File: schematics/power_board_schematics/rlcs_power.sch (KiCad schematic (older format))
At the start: 40 parts, among them J1 SD_Card, J2 Battery Conn, J3 CONN_01X02, J4 CONN_01X02, J5 CONN_01X02, J6 CONN_01X02, Q4 Q_NPN_BEC, Q5 Q_NPN_BEC, T1 12 to 3v3, T2 12 to 5

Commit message: Added more connections
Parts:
- renumbered Header to Header1
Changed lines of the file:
@@
 $EndComp
-$Comp
-L Device:R_Small R2
-U 1 1 59C44DB4
-P 3450 4900
-F 0 "R2" V 3450 4850 50  0000 L CNN
-F 1 "150" V 3500 4850 50  0001 L CNN
-F 2 "Resistors_SMD:R_0805_HandSoldering" H 3450 4900 50  0001 C CNN
-F 3 "" H 3450 4900 50  0001 C CNN
-	1    3450 4900
-	0    -1   -1   0
-$EndComp
-Text Notes 3200 4800 0    60   ~ 0
-100ohm\nresistors\n
 $Comp
 L Device:Jumper_NC_Dual JP1
@@
 	1    4750 1350
 	1    0    0    -1
-$EndComp
-$Comp
-L Device:R_Small R3
-U 1 1 59C5B971
-P 3450 5000
-F 0 "R3" V 3450 4950 50  0000 L CNN
-F 1 "150" V 3500 4950 50  0001 L CNN
-F 2 "Resistors_SMD:R_0805_HandSoldering" H 3450 5000 50  0001 C CNN
-F 3 "" H 3450 5000 50  0001 C CNN
-	1    3450 5000
-	0    -1   -1   0
-$EndComp
-$Comp
-L custom:LTD-4608JR AFF1
-U 1 1 59C5BADA
-P 4300 5300
-F 0 "AFF1" H 3950 4800 50  0000 C CNN
-F 1 "LTD-4608JR" H 4600 4800 50  0000 C CNN
-F 2 "rlcs_power:LTD-4608JR" H 4300 5300 50  0001 C CNN
-F 3 "" H 4300 5300 50  0001 C CNN
-	1    4300 5300
-	0    -1   -1   0
-$EndComp
-$Comp
-L Device:R_Small R4
-U 1 1 59C5BB74
-P 3450 5100
-F 0 "R4" V 3450 5050 50  0000 L CNN
-F 1 "150" V 3500 5050 50  0001 L CNN
-F 2 "Resistors_SMD:R_0805_HandSoldering" H 3450 5100 50  0001 C CNN
-F 3 "" H 3450 5100 50  0001 C CNN
-	1    3450 5100
-	0    -1   -1   0
-$EndComp
-$Comp
-L Device:R_Small R5
-U 1 1 59C5BC0E
-P 3450 5200
-F 0 "R5" V 3450 5150 50  0000 L CNN
-F 1 "150" V 3500 5150 50  0001 L CNN
-F 2 "Resistors_SMD:R_0805_HandSoldering" H 3450 5200 50  0001 C CNN
-F 3 "" H 3450 5200 50  0001 C CNN
-	1    3450 5200
-	0    -1   -1   0
-$EndComp
-$Comp
-L Device:R_Small R6
-U 1 1 59C5BCA9
-P 3450 5300
-F 0 "R6" V 3450 5250 50  0000 L CNN
-F 1 "150" V 3500 5250 50  0001 L CNN
-F 2 "Resistors_SMD:R_0805_HandSoldering" H 3450 5300 50  0001 C CNN
-F 3 "" H 3450 5300 50  0001 C CNN
-	1    3450 5300
-	0    -1   -1   0
-$EndComp
-$Comp
-L Device:R_Small R7
-U 1 1 59C5BD47
-P 3450 5400
-F 0 "R7" V 3450 5350 50  0000 L CNN
-F 1 "150" V 3500 5350 50  0001 L CNN
-F 2 "Resistors_SMD:R_0805_HandSoldering" H 3450 5400 50  0001 C CNN
-F 3 "" H 3450 5400 50  0001 C CNN
-	1    3450 5400
-	0    -1   -1   0
-$EndComp
-$Comp
-L Device:R_Small R8
-U 1 1 59C5BDE8
-P 3450 5500
-F 0 "R8" V 3450 5450 50  0000 L CNN
-F 1 "150" V 3500 5450 50  0001 L CNN
-F 2 "Resistors_SMD:R_0805_HandSoldering" H 3450 5500 50  0001 C CNN
-F 3 "" H 3450 5500 50  0001 C CNN
-	1    3450 5500
-	0    -1   -1   0
-$EndComp
-$Comp
-L Device:R_Small R9
-U 1 1 59C5BE8C
-P 3450 5750
-F 0 "R9" V 3450 5700 50  0000 L CNN
-F 1 "150" V 3500 5700 50  0001 L CNN
-F 2 "Resistors_SMD:R_0805_HandSoldering" H 3450 5750 50  0001 C CNN
-F 3 "" H 3450 5750 50  0001 C CNN
-	1    3450 5750
-	0    -1   -1   0
 $EndComp
 $Comp
@@
 Text GLabel 1950 3900 0    60   Input ~ 0
 ARD_CON_7SEG_D1
-Text GLabel 2000 6400 0    60   Input ~ 0
-ARD_CON_7SEG_D2
 $Comp
 L rlcs_power-rescue:TEST_1P TP3
@@
 $EndComp
 $Comp
-L Device:Q_NPN_BEC Q4
-U 1 1 59CA1E66
-P 3550 6400
-F 0 "Q4" H 3750 6450 50  0000 L CNN
-F 1 "Q_NPN_BEC" H 3750 6350 50  0000 L CNN
-F 2 "TO_SOT_Packages_SMD:SOT-23_Handsoldering" H 3750 6500 50  0001 C CNN
-F 3 "" H 3550 6400 50  0001 C CNN
-	1    3550 6400
-	1    0    0    -1
-$EndComp
-$Comp
 L Device:Q_NPN_BEC Q5
 U 1 1 59CA20EF
@@
 F 3 "" H 4400 3700 50  0001 C CNN
 	1    4400 3700
-	1    0    0    -1
-$EndComp
-$Comp
-L power:+5V #PWR023
-U 1 1 59CA27CE
-P 3650 6200
-F 0 "#PWR023" H 3650 6050 50  0001 C CNN
-F 1 "+5V" H 3650 6340 50  0000 C CNN
-F 2 "" H 3650 6200 50  0001 C CNN
-F 3 "" H 3650 6200 50  0001 C CNN
-	1    3650 6200
 	1    0    0    -1
 $EndComp
@@
 Wire Wire Line
 	1950 2550 2750 2550
-Wire Wire Line
-	2000 6400 3350 6400
-Wire Wire Line
-	4400 4100 4400 4450
-Wire Wire Line
-	1950 3900 4100 3900
-Wire Wire Line
-	3650 6600 4250 6600
-Wire Wire Line
-	4250 6600 4250 6150
 Connection ~ 4450 1050
 Wire Wire Line
@@
 Wire Wire Line
 	3200 2550 3850 2550
-$Comp
-L Connector:Conn_01x08_Male Header
+Wire Wire Line
+	1950 3900 4100 3900
+$Comp
+L custom:LTD-4608JR AFF1
+U 1 1 59C5BADA
+P 4300 5300
+F 0 "AFF1" H 3950 4800 50  0000 C CNN
+F 1 "LTD-4608JR" H 4600 4800 50  0000 C CNN
+F 2 "rlcs_power:LTD-4608JR" H 4300 5300 50  0001 C CNN
+F 3 "" H 4300 5300 50  0001 C CNN
+	1    4300 5300
+	0    -1   -1   0
+$EndComp
+Wire Wire Line
+	2750 5750 2750 5600
+Wire Wire Line
+	3350 5750 2750 5750
+Wire Wire Line
+	3350 5500 2750 5500
+Wire Wire Line
+	3350 5400 2750 5400
+Wire Wire Line
+	3350 5300 2750 5300
+Wire Wire Line
+	3350 5200 2750 5200
+Wire Wire Line
+	3350 5100 2750 5100
+Wire Wire Line
+	3350 5000 2750 5000
+Wire Wire Line
+	3350 4900 2750 4900
+$Comp
+L Connector:Conn_01x08_Male Header1
 U 1 1 5E6E5A01
 P 2550 5200
-F 0 "Header" H 2658 5681 50  0000 C CNN
+F 0 "Header1" H 2658 5681 50  0000 C CNN
 F 1 "Conn_01x08_Male" H 2658 5590 50  0000 C CNN
 F 2 "" H 2550 5200 50  0001 C CNN
@@
 $EndComp
 Wire Wire Line
-	3350 4900 2750 4900
-Wire Wire Line
-	3350 5000 2750 5000
-Wire Wire Line
-	3350 5100 2750 5100
-Wire Wire Line
-	3350 5200 2750 5200
-Wire Wire Line
-	3350 5300 2750 5300
-Wire Wire Line
-	3350 5400 2750 5400
-Wire Wire Line
-	3350 5500 2750 5500
-Wire Wire Line
-	3350 5750 2750 5750
-Wire Wire Line
-	2750 5750 2750 5600
+	4250 6600 4250 6150
+Wire Wire Line
+	3650 6600 4250 6600
+Wire Wire Line
+	4400 4100 4400 4450
+Wire Wire Line
+	2000 6400 3350 6400
+$Comp
+L power:+5V #PWR023
+U 1 1 59CA27CE
+P 3650 6200
+F 0 "#PWR023" H 3650 6050 50  0001 C CNN
+F 1 "+5V" H 3650 6340 50  0000 C CNN
+F 2 "" H 3650 6200 50  0001 C CNN
+F 3 "" H 3650 6200 50  0001 C CNN
+	1    3650 6200
+	1    0    0    -1
+$EndComp
+$Comp
+L Device:Q_NPN_BEC Q4
+U 1 1 59CA1E66
+P 3550 6400
+F 0 "Q4" H 3750 6450 50  0000 L CNN
+F 1 "Q_NPN_BEC" H 3750 6350 50  0000 L CNN
+F 2 "TO_SOT_Packages_SMD:SOT-23_Handsoldering" H 3750 6500 50  0001 C CNN
+F 3 "" H 3550 6400 50  0001 C CNN
+	1    3550 6400
+	1    0    0    -1
+$EndComp
+Text GLabel 2000 6400 0    60   Input ~ 0
+ARD_CON_7SEG_D2
+$Comp
+L Device:R_Small R9
+U 1 1 59C5BE8C
+P 3450 5750
+F 0 "R9" V 3450 5700 50  0000 L CNN
+F 1 "150" V 3500 5700 50  0001 L CNN
+F 2 "Resistors_SMD:R_0805_HandSoldering" H 3450 5750 50  0001 C CNN
+F 3 "" H 3450 5750 50  0001 C CNN
+	1    3450 5750
+	0    -1   -1   0
+$EndComp
+$Comp
+L Device:R_Small R8
+U 1 1 59C5BDE8
+P 3450 5500
+F 0 "R8" V 3450 5450 50  0000 L CNN
+F 1 "150" V 3500 5450 50  0001 L CNN
+F 2 "Resistors_SMD:R_0805_HandSoldering" H 3450 5500 50  0001 C CNN
+F 3 "" H 3450 5500 50  0001 C CNN
+	1    3450 5500
+	0    -1   -1   0
+$EndComp
+$Comp
+L Device:R_Small R7
+U 1 1 59C5BD47
+P 3450 5400
+F 0 "R7" V 3450 5350 50  0000 L CNN
+F 1 "150" V 3500 5350 50  0001 L CNN
+F 2 "Resistors_SMD:R_0805_HandSoldering" H 3450 5400 50  0001 C CNN
+F 3 "" H 3450 5400 50  0001 C CNN
+	1    3450 5400
+	0    -1   -1   0
+$EndComp
+$Comp
+L Device:R_Small R6
+U 1 1 59C5BCA9
+P 3450 5300
+F 0 "R6" V 3450 5250 50  0000 L CNN
+F 1 "150" V 3500 5250 50  0001 L CNN
+F 2 "Resistors_SMD:R_0805_HandSoldering" H 3450 5300 50  0001 C CNN
+F 3 "" H 3450 5300 50  0001 C CNN
+	1    3450 5300
+	0    -1   -1   0
+$EndComp
+$Comp
+L Device:R_Small R5
+U 1 1 59C5BC0E
+P 3450 5200
+F 0 "R5" V 3450 5150 50  0000 L CNN
+F 1 "150" V 3500 5150 50  0001 L CNN
+F 2 "Resistors_SMD:R_0805_HandSoldering" H 3450 5200 50  0001 C CNN
+F 3 "" H 3450 5200 50  0001 C CNN
+	1    3450 5200
+	0    -1   -1   0
+$EndComp
+$Comp
+L Device:R_Small R4
+U 1 1 59C5BB74
+P 3450 5100
+F 0 "R4" V 3450 5050 50  0000 L CNN
+F 1 "150" V 3500 5050 50  0001 L CNN
+F 2 "Resistors_SMD:R_0805_HandSoldering" H 3450 5100 50  0001 C CNN
+F 3 "" H 3450 5100 50  0001 C CNN
+	1    3450 5100
+	0    -1   -1   0
+$EndComp
+$Comp
+L Device:R_Small R3
+U 1 1 59C5B971
+P 3450 5000
+F 0 "R3" V 3450 4950 50  0000 L CNN
+F 1 "150" V 3500 4950 50  0001 L CNN
+F 2 "Resistors_SMD:R_0805_HandSoldering" H 3450 5000 50  0001 C CNN
+F 3 "" H 3450 5000 50  0001 C CNN
+	1    3450 5000
+	0    -1   -1   0
+$EndComp
+Text Notes 3200 4800 0    60   ~ 0
+100ohm\nresistors\n
+$Comp
+L Device:R_Small R2
+U 1 1 59C44DB4
+P 3450 4900
+F 0 "R2" V 3450 4850 50  0000 L CNN
+F 1 "150" V 3500 4850 50  0001 L CNN
+F 2 "Resistors_SMD:R_0805_HandSoldering" H 3450 4900 50  0001 C CNN
+F 3 "" H 3450 4900 50  0001 C CNN
+	1    3450 4900
+	0    -1   -1   0
+$EndComp
 $EndSCHEMATC

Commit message: First commit
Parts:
- removed Header1: Conn_01x08_Male, symbol Connector:Conn_01x08_Male
- removed J5: CONN_01X02, Connectors_Molex:Molex_KK-6410-02_02x2.54mm_Straight, symbol rlcs_power-rescue:CONN_01X02
- added J?: Conn_01x05_Female, symbol Connector:Conn_01x05_Female
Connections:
- net +5V: now also J?.1 (Pin_1), J?.2 (Pin_2)
- net GND: now also J?.3 (Pin_3), J?.4 (Pin_4), J?.5 (Pin_5)
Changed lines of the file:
@@
-$EndComp
-$Comp
-L power:+15V #PWR017
-U 1 1 59C65520
-P 9900 5950
-F 0 "#PWR017" H 9900 5800 50  0001 C CNN
-F 1 "+15V" H 9900 6090 50  0000 C CNN
-F 2 "" H 9900 5950 50  0001 C CNN
-F 3 "" H 9900 5950 50  0001 C CNN
-	1    9900 5950
-	1    0    0    -1
 $EndComp
 $Comp
@@
 $EndComp
 $Sheet
-S 850  6950 1150 600
+S 900  7100 1150 600
 U 59C6DB4C
 F0 "Arduino Connections" 60
@@
 Text GLabel 1950 3100 0    60   Input ~ 0
 ARD_CON_SD_MISO
-Text GLabel 1950 3900 0    60   Input ~ 0
-ARD_CON_7SEG_D1
 $Comp
 L rlcs_power-rescue:TEST_1P TP3
@@
 $EndComp
 $Comp
-L rlcs_power-rescue:CONN_01X02 J5
-U 1 1 59C7C50E
-P 10200 6050
-F 0 "J5" H 10200 6200 50  0000 C CNN
-F 1 "CONN_01X02" V 10300 6050 50  0000 C CNN
-F 2 "Connectors_Molex:Molex_KK-6410-02_02x2.54mm_Straight" H 10200 6050 50  0001 C CNN
-F 3 "" H 10200 6050 50  0001 C CNN
-	1    10200 6050
-	1    0    0    -1
-$EndComp
-$Comp
 L power:+5V #PWR019
 U 1 1 59C84289
@@
 	10450 1850 10450 1800
 Wire Wire Line
-	10000 6000 9900 6000
-Wire Wire Line
-	9900 6000 9900 5950
-Wire Wire Line
-	10000 6100 9900 6100
-Wire Wire Line
-	9900 6100 9900 6150
-Wire Wire Line
 	10000 5500 9900 5500
 Wire Wire Line
@@
 Wire Wire Line
 	9050 2050 9400 2050
-$Comp
-L power:GNDREF #PWR026
-U 1 1 59D5CCF0
-P 9900 6150
-F 0 "#PWR026" H 9900 5900 50  0001 C CNN
-F 1 "GNDREF" H 9900 6000 50  0000 C CNN
-F 2 "" H 9900 6150 50  0001 C CNN
-F 3 "" H 9900 6150 50  0001 C CNN
-	1    9900 6150
-	1    0    0    -1
-$EndComp
 $Comp
 L Device:R R15
@@
 $EndComp
 Wire Wire Line
-	2750 5750 2750 5600
-Wire Wire Line
-	3350 5750 2750 5750
-Wire Wire Line
-	3350 5500 2750 5500
-Wire Wire Line
-	3350 5400 2750 5400
-Wire Wire Line
-	3350 5300 2750 5300
-Wire Wire Line
-	3350 5200 2750 5200
-Wire Wire Line
-	3350 5100 2750 5100
-Wire Wire Line
-	3350 5000 2750 5000
-Wire Wire Line
-	3350 4900 2750 4900
-$Comp
-L Connector:Conn_01x08_Male Header1
-U 1 1 5E6E5A01
-P 2550 5200
-F 0 "Header1" H 2658 5681 50  0000 C CNN
-F 1 "Conn_01x08_Male" H 2658 5590 50  0000 C CNN
-F 2 "" H 2550 5200 50  0001 C CNN
-F 3 "~" H 2550 5200 50  0001 C CNN
-	1    2550 5200
-	1    0    0    -1
-$EndComp
-Wire Wire Line
 	4250 6600 4250 6150
 Wire Wire Line
@@
 	0    -1   -1   0
 $EndComp
+Text GLabel 1950 3900 0    60   Input ~ 0
+ARD_CON_7SEG_D1
+$Comp
+L Connector:Conn_01x05_Female J?
+U 1 1 5EBB93B2
+P 6850 4750
+F 0 "J?" H 6878 4776 50  0000 L CNN
+F 1 "Conn_01x05_Female" H 6878 4685 50  0000 L CNN
+F 2 "" H 6850 4750 50  0001 C CNN
+F 3 "~" H 6850 4750 50  0001 C CNN
+	1    6850 4750
+	-1   0    0    -1
+$EndComp
+Wire Wire Line
+	7050 4550 7450 4550
+Wire Wire Line
+	7050 4650 7450 4650
+Wire Wire Line
+	7050 4750 7450 4750
+Wire Wire Line
+	7050 4850 7450 4850
+Wire Wire Line
+	7050 4950 7450 4950
+Wire Wire Line
+	7450 4650 7450 4550
+Connection ~ 7450 4550
+Wire Wire Line
+	7450 4550 7450 4400
+Wire Wire Line
+	7450 4750 7450 4850
+Connection ~ 7450 4850
+Wire Wire Line
+	7450 4850 7450 4950
+Connection ~ 7450 4950
+Wire Wire Line
+	7450 4950 7450 5150
+Wire Wire Line
+	7450 4850 7700 4850
+Wire Wire Line
+	7450 4950 7700 4950
+Wire Wire Line
+	7450 4550 7700 4550
+$Comp
+L power:GND #PWR?
+U 1 1 5EBFE204
+P 7450 5150
+F 0 "#PWR?" H 7450 4900 50  0001 C CNN
+F 1 "GND" H 7455 4977 50  0000 C CNN
+F 2 "" H 7450 5150 50  0001 C CNN
+F 3 "" H 7450 5150 50  0001 C CNN
+	1    7450 5150
+	1    0    0    -1
+$EndComp
+$Comp
+L power:+5V #PWR?
+U 1 1 5EBFECC0
+P 7450 4400
+F 0 "#PWR?" H 7450 4250 50  0001 C CNN
+F 1 "+5V" H 7465 4573 50  0000 C CNN
+F 2 "" H 7450 4400 50  0001 C CNN
+F 3 "" H 7450 4400 50  0001 C CNN
+	1    7450 4400
+	1    0    0    -1
+$EndComp
+Text Label 7700 4550 0    60   ~ 0
+MCLR
+Text Label 7700 4850 0    60   ~ 0
+ICSPDAT
+Text Label 7700 4950 0    60   ~ 0
+ICSPCLK
 $EndSCHEMATC

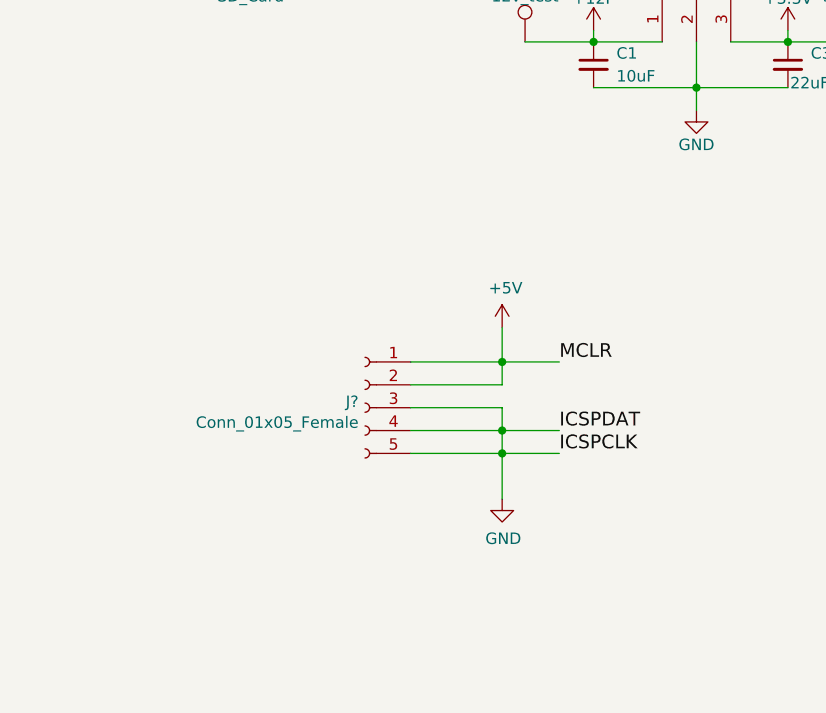
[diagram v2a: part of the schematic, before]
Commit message: Set CD and WP to 54 and 55 respectively
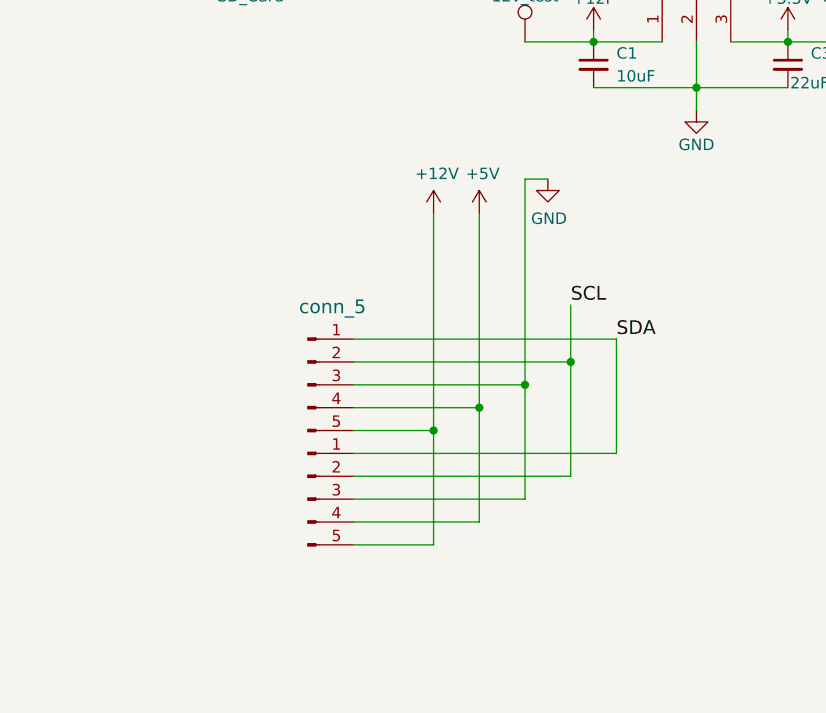
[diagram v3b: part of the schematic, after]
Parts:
- removed J?: Conn_01x05_Female, symbol Connector:Conn_01x05_Female
- added ~: conn_5, symbol custom:conn_5
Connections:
- net +5V: now also ~.4
- net GND: now also ~.3
- new net +12V: ~.5
- new net SCL: ~.2
- new net SDA: ~.1
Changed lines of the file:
@@
 ARD_CON_7SEG_D1
 $Comp
-L Connector:Conn_01x05_Female J?
-U 1 1 5EBB93B2
-P 6850 4750
-F 0 "J?" H 6878 4776 50  0000 L CNN
-F 1 "Conn_01x05_Female" H 6878 4685 50  0000 L CNN
-F 2 "" H 6850 4750 50  0001 C CNN
-F 3 "~" H 6850 4750 50  0001 C CNN
-	1    6850 4750
-	-1   0    0    -1
+L custom:conn_5 ~
+U 1 1 5ECEAAD4
+P 6750 4850
+F 0 "~" H 6708 5497 60  0000 C CNN
+F 1 "conn_5" H 6708 5391 60  0000 C CNN
+F 2 "" H 6750 5450 60  0001 C CNN
+F 3 "" H 6750 5450 60  0001 C CNN
+	1    6750 4850
+	1    0    0    -1
 $EndComp
 Wire Wire Line
-	7050 4550 7450 4550
+	7150 5350 7150 4850
 Wire Wire Line
-	7050 4650 7450 4650
+	6800 5350 7150 5350
 Wire Wire Line
-	7050 4750 7450 4750
+	7550 3750 7650 3750
 Wire Wire Line
-	7050 4850 7450 4850
+	6800 4850 7150 4850
+Connection ~ 7150 4850
 Wire Wire Line
-	7050 4950 7450 4950
-Wire Wire Line
-	7450 4650 7450 4550
-Connection ~ 7450 4550
-Wire Wire Line
-	7450 4550 7450 4400
-Wire Wire Line
-	7450 4750 7450 4850
-Connection ~ 7450 4850
-Wire Wire Line
-	7450 4850 7450 4950
-Connection ~ 7450 4950
-Wire Wire Line
-	7450 4950 7450 5150
-Wire Wire Line
-	7450 4850 7700 4850
-Wire Wire Line
-	7450 4950 7700 4950
-Wire Wire Line
-	7450 4550 7700 4550
+	7150 4850 7150 3900
 $Comp
-L power:GND #PWR?
-U 1 1 5EBFE204
-P 7450 5150
-F 0 "#PWR?" H 7450 4900 50  0001 C CNN
-F 1 "GND" H 7455 4977 50  0000 C CNN
-F 2 "" H 7450 5150 50  0001 C CNN
-F 3 "" H 7450 5150 50  0001 C CNN
-	1    7450 5150
+L power:+12V #PWR?
+U 1 1 5ED2A677
+P 7150 3900
+F 0 "#PWR?" H 7150 3750 50  0001 C CNN
+F 1 "+12V" H 7165 4073 50  0000 C CNN
+F 2 "" H 7150 3900 50  0001 C CNN
+F 3 "" H 7150 3900 50  0001 C CNN
+	1    7150 3900
 	1    0    0    -1
 $EndComp
 $Comp
 L power:+5V #PWR?
-U 1 1 5EBFECC0
-P 7450 4400
-F 0 "#PWR?" H 7450 4250 50  0001 C CNN
-F 1 "+5V" H 7465 4573 50  0000 C CNN
-F 2 "" H 7450 4400 50  0001 C CNN
-F 3 "" H 7450 4400 50  0001 C CNN
-	1    7450 4400
+U 1 1 5ED2ACA3
+P 7350 3900
+F 0 "#PWR?" H 7350 3750 50  0001 C CNN
+F 1 "+5V" H 7365 4073 50  0000 C CNN
+F 2 "" H 7350 3900 50  0001 C CNN
+F 3 "" H 7350 3900 50  0001 C CNN
+	1    7350 3900
 	1    0    0    -1
 $EndComp
-Text Label 7700 4550 0    60   ~ 0
-MCLR
-Text Label 7700 4850 0    60   ~ 0
-ICSPDAT
-Text Label 7700 4950 0    60   ~ 0
-ICSPCLK
+Wire Wire Line
+	6800 5050 7750 5050
+Wire Wire Line
+	6800 5150 7550 5150
+Wire Wire Line
+	6800 5250 7350 5250
+Wire Wire Line
+	7350 3900 7350 4750
+Wire Wire Line
+	7550 3750 7550 4650
+Wire Wire Line
+	6800 4750 7350 4750
+Connection ~ 7350 4750
+Wire Wire Line
+	7350 4750 7350 5250
+Wire Wire Line
+	6800 4650 7550 4650
+Connection ~ 7550 4650
+Wire Wire Line
+	7550 4650 7550 5150
+$Comp
+L power:GND #PWR?
+U 1 1 5ED75BA3
+P 7650 3750
+F 0 "#PWR?" H 7650 3500 50  0001 C CNN
+F 1 "GND" H 7655 3577 50  0000 C CNN
+F 2 "" H 7650 3750 50  0001 C CNN
+F 3 "" H 7650 3750 50  0001 C CNN
+	1    7650 3750
+	1    0    0    -1
+$EndComp
+Wire Wire Line
+	6800 4550 7750 4550
+Wire Wire Line
+	7750 4550 7750 5050
+Wire Wire Line
+	6800 4450 7950 4450
+Wire Wire Line
+	7950 4450 7950 4950
+Wire Wire Line
+	7950 4950 6800 4950
+Text Label 7750 4300 0    60   ~ 0
+SCL
+Text Label 7950 4450 0    60   ~ 0
+SDA
+Wire Wire Line
+	7750 4550 7750 4300
+Connection ~ 7750 4550
 $EndSCHEMATC
